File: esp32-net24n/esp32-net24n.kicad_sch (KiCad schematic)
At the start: 6 parts, among them U1 OKI-78SR-3.3_1.5-W36-C, U2 ESP32-S2

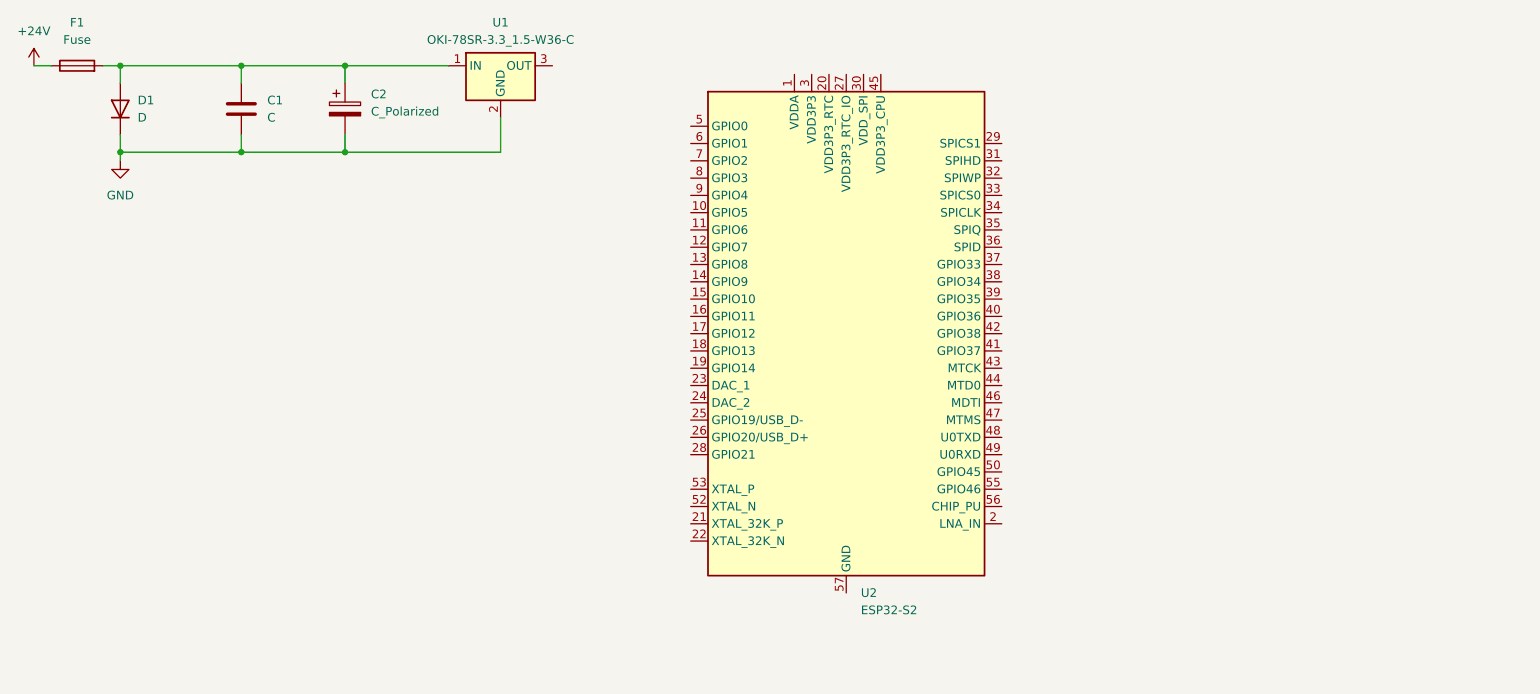
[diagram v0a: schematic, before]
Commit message: Added azdelivery symbol collection.
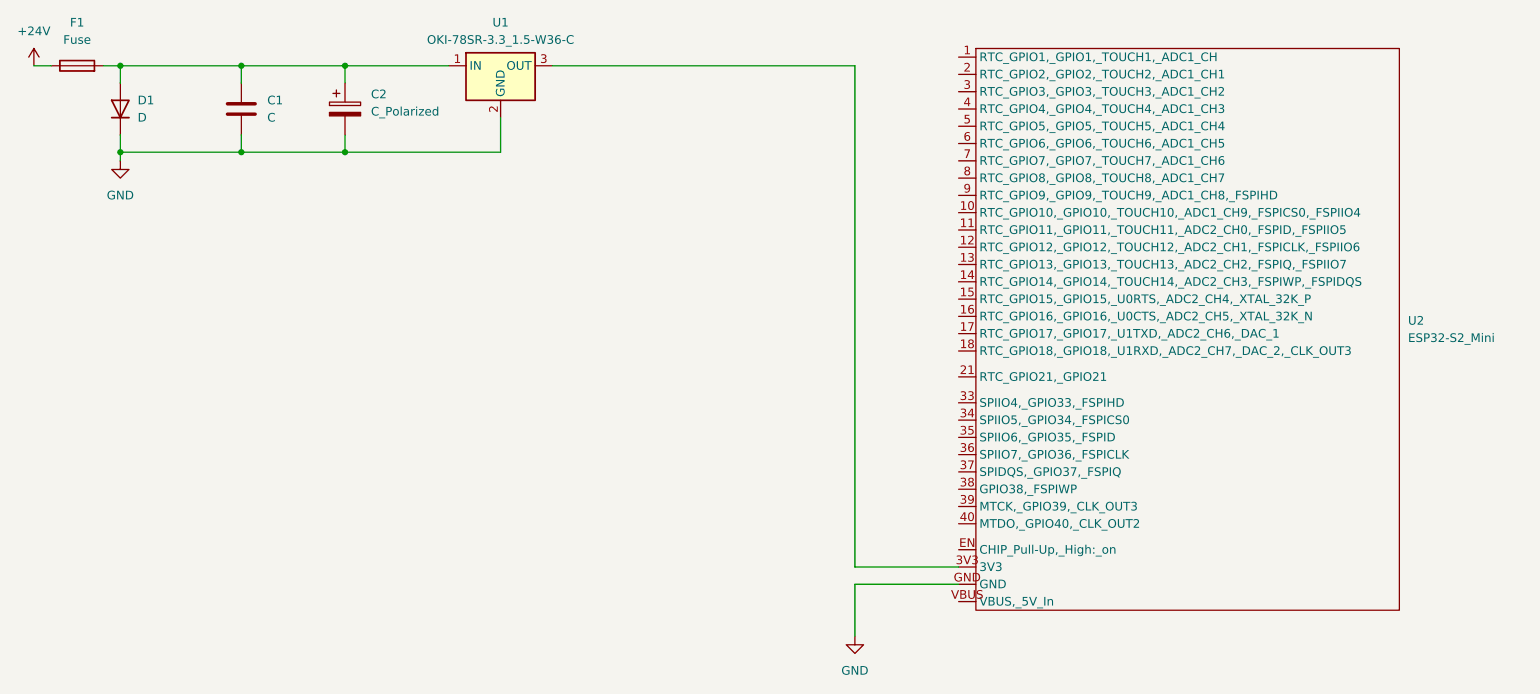
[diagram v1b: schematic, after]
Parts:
- removed U2: ESP32-S2, Package_DFN_QFN:QFN-56-1EP_7x7mm_P0.4mm_EP4x4mm, symbol MCU_Espressif:ESP32-S2
- added U2: ESP32-S2_Mini, AZDelivery:ESP32-S2-Mini, symbol AZDelivery:ESP32-S2_Mini
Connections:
- net GND: now also U2.GND
- net at U1.3 (OUT): now also U2.3V3
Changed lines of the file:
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@@
+	(wire
+		(pts
+			(xy 166.37 130.81) (xy 166.37 138.43)
+		)
+		(stroke
+			(width 0)
+			(type default)
+		)
+	)
 	(wire
 		(pts
@@
 	(wire
 		(pts
+			(xy 181.61 130.81) (xy 166.37 130.81)
+		)
+		(stroke
+			(width 0)
+			(type default)
+		)
+	)
+	(wire
+		(pts
 			(xy 76.2 64.77) (xy 76.2 67.31)
 		)
@@
 	(wire
 		(pts
+			(xy 121.92 54.61) (xy 166.37 54.61)
+		)
+		(stroke
+			(width 0)
+			(type default)
+		)
+	)
+	(wire
+		(pts
+			(xy 166.37 54.61) (xy 166.37 128.27)
+		)
+		(stroke
+			(width 0)
+			(type default)
+		)
+	)
+	(wire
+		(pts
 			(xy 91.44 54.61) (xy 106.68 54.61)
 		)
@@
 	(wire
 		(pts
+			(xy 166.37 128.27) (xy 181.61 128.27)
+		)
+		(stroke
+			(width 0)
+			(type default)
+		)
+	)
+	(wire
+		(pts
 			(xy 114.3 67.31) (xy 91.44 67.31)
 		)
@@
 	)
 	(symbol
-		(lib_id "MCU_Espressif:ESP32-S2")
-		(at 165.1 93.98 0)
+		(lib_id "power:GND")
+		(at 166.37 138.43 0)
 		(unit 1)
 		(body_style 1)
@@
 		(dnp no)
 		(fields_autoplaced yes)
-		(property "Reference" "U2"
-			(at 167.2433 132.08 0)
-			(show_name no)
-			(do_not_autoplace no)
-			(effects
-				(font
-					(size 1.27 1.27)
-				)
-				(justify left)
-			)
-		)
-		(property "Value" "ESP32-S2"
-			(at 167.2433 134.62 0)
-			(show_name no)
-			(do_not_autoplace no)
-			(effects
-				(font
-					(size 1.27 1.27)
-				)
-				(justify left)
-			)
-		)
-		(property "Footprint" "Package_DFN_QFN:QFN-56-1EP_7x7mm_P0.4mm_EP4x4mm"
-			(at 167.64 142.24 0)
-			(hide yes)
-			(show_name no)
-			(do_not_autoplace no)
-			(effects
-				(font
-					(size 1.27 1.27)
-				)
-				(justify left)
-			)
-		)
-		(property "Datasheet" "https://www.espressif.com/sites/default/files/documentation/esp32-s2_datasheet_en.pdf"
-			(at 167.64 139.7 0)
-			(hide yes)
-			(show_name no)
-			(do_not_autoplace no)
-			(effects
-				(font
-					(size 1.27 1.27)
-				)
-				(justify left)
-			)
-		)
-		(property "Description" "Microcontroller, Wi-Fi 802.11b/g/n, Bluetooth, 32bit"
-			(at 165.1 93.98 0)
-			(hide yes)
-			(show_name no)
-			(do_not_autoplace no)
-			(effects
-				(font
-					(size 1.27 1.27)
-				)
-			)
-		)
-		(pin "39"
-		)
-		(pin "18"
-		)
-		(pin "38"
-		)
-		(pin "22"
-		)
-		(pin "32"
-		)
-		(pin "13"
-		)
-		(pin "35"
-		)
-		(pin "48"
-		)
-		(pin "23"
-		)
-		(pin "53"
-		)
-		(pin "15"
-		)
-		(pin "45"
-		)
-		(pin "36"
-		)
-		(pin "44"
-		)
-		(pin "54"
-		)
-		(pin "16"
-		)
-		(pin "37"
-		)
-		(pin "19"
-		)
-		(pin "20"
-		)
-		(pin "21"
-		)
-		(pin "28"
-		)
-		(pin "50"
-		)
-		(pin "26"
-		)
-		(pin "52"
-		)
-		(pin "17"
-		)
-		(pin "27"
-		)
-		(pin "33"
-		)
-		(pin "49"
-		)
-		(pin "31"
-		)
-		(pin "25"
-		)
-		(pin "47"
-		)
-		(pin "55"
-		)
-		(pin "29"
-		)
-		(pin "24"
-		)
-		(pin "14"
-		)
-		(pin "30"
-		)
-		(pin "42"
-		)
-		(pin "51"
-		)
-		(pin "40"
-		)
-		(pin "34"
-		)
-		(pin "41"
-		)
-		(pin "57"
-		)
-		(pin "56"
-		)
-		(pin "43"
-		)
-		(pin "46"
-		)
-		(pin "12"
-		)
-		(pin "11"
-		)
-		(pin "10"
-		)
-		(pin "9"
-		)
-		(pin "8"
-		)
-		(pin "7"
-		)
-		(pin "6"
-		)
-		(pin "5"
-		)
-		(pin "4"
-		)
-		(pin "3"
-		)
-		(pin "2"
+		(property "Reference" "#PWR03"
+			(at 166.37 144.78 0)
+			(hide yes)
+			(show_name no)
+			(do_not_autoplace no)
+			(effects
+				(font
+					(size 1.27 1.27)
+				)
+			)
+		)
+		(property "Value" "GND"
+			(at 166.37 143.51 0)
+			(show_name no)
+			(do_not_autoplace no)
+			(effects
+				(font
+					(size 1.27 1.27)
+				)
+			)
+		)
+		(property "Footprint" ""
+			(at 166.37 138.43 0)
+			(hide yes)
+			(show_name no)
+			(do_not_autoplace no)
+			(effects
+				(font
+					(size 1.27 1.27)
+				)
+			)
+		)
+		(property "Datasheet" ""
+			(at 166.37 138.43 0)
+			(hide yes)
+			(show_name no)
+			(do_not_autoplace no)
+			(effects
+				(font
+					(size 1.27 1.27)
+				)
+			)
+		)
+		(property "Description" "Power symbol creates a global label with name \"GND\" , ground"
+			(at 166.37 138.43 0)
+			(hide yes)
+			(show_name no)
+			(do_not_autoplace no)
+			(effects
+				(font
+					(size 1.27 1.27)
+				)
+			)
 		)
 		(pin "1"
@@
 			(project "esp32-net24n"
 				(path "/3ee1fc5b-dadf-4870-a8bf-d1f3f1ab1720"
-					(reference "U2")
+					(reference "#PWR03")
 					(unit 1)
 				)
@@
 					(unit 1)
 				)
+			)
+		)
+	)
+	(symbol
+		(lib_id "AZDelivery:ESP32-S2_Mini")
+		(at 181.61 53.34 0)
+		(unit 1)
+		(body_style 1)
+		(exclude_from_sim no)
+		(in_bom yes)
+		(on_board yes)
+		(in_pos_files yes)
+		(dnp no)
+		(fields_autoplaced yes)
+		(property "Reference" "U2"
+			(at 247.65 92.0749 0)
+			(show_name no)
+			(do_not_autoplace no)
+			(effects
+				(font
+					(size 1.27 1.27)
+				)
+				(justify left)
+			)
+		)
+		(property "Value" "ESP32-S2_Mini"
+			(at 247.65 94.6149 0)
+			(show_name no)
+			(do_not_autoplace no)
+			(effects
+				(font
+					(size 1.27 1.27)
+				)
+				(justify left)
+			)
+		)
+		(property "Footprint" "AZDelivery:ESP32-S2-Mini"
+			(at 181.61 53.34 0)
+			(hide yes)
+			(show_name no)
+			(do_not_autoplace no)
+			(effects
+				(font
+					(size 1.27 1.27)
+				)
+			)
+		)
+		(property "Datasheet" ""
+			(at 181.61 53.34 0)
+			(hide yes)
+			(show_name no)
+			(do_not_autoplace no)
+			(effects
+				(font
+					(size 1.27 1.27)
+				)
+			)
+		)
+		(property "Description" ""
+			(at 181.61 53.34 0)
+			(hide yes)
+			(show_name no)
+			(do_not_autoplace no)
+			(effects
+				(font
+					(size 1.27 1.27)
+				)
+			)
+		)
+		(pin "6"
+		)
+		(pin "35"
+		)
+		(pin "34"
+		)
+		(pin "39"
+		)
+		(pin "VBUS"
+		)
+		(pin "EN"
+		)
+		(pin "36"
+		)
+		(pin "8"
+		)
+		(pin "5"
+		)
+		(pin "40"
+		)
+		(pin "12"
+		)
+		(pin "13"
+		)
+		(pin "2"
+		)
+		(pin "3"
+		)
+		(pin "18"
+		)
+		(pin "11"
+		)
+		(pin "33"
+		)
+		(pin "3V3"
+		)
+		(pin "37"
+		)
+		(pin "21"
+		)
+		(pin "7"
+		)
+		(pin "16"
+		)
+		(pin "1"
+		)
+		(pin "4"
+		)
+		(pin "17"
+		)
+		(pin "10"
+		)
+		(pin "GND"
+		)
+		(pin "38"
+		)
+		(pin "14"
+		)
+		(pin "9"
+		)
+		(pin "15"
+		)
+		(instances
+			(project "esp32-net24n"
+				(path "/3ee1fc5b-dadf-4870-a8bf-d1f3f1ab1720"
+					(reference "U2")
+					(unit 1)
+				)
